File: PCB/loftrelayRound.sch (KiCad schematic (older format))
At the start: 29 parts, among them J1 PowerIn, J2 Load, J3 SenSor, J4 Program, K1 G5Q-14-EU DC5, Q1 2N7002, U1 AP1117-33, U2 PC817, U4 ESP-12E

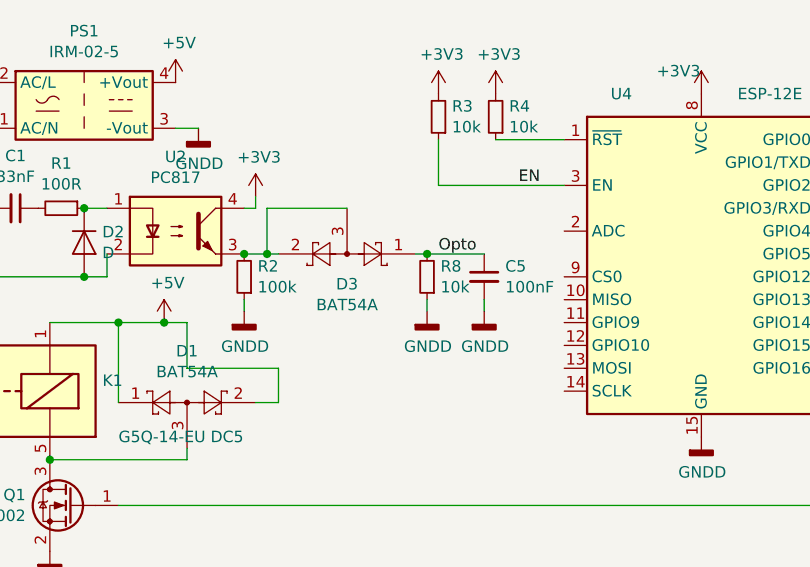
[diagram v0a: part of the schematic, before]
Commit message: Diagram rettet til
Minimeret, så overflødige komponenter er fjernet
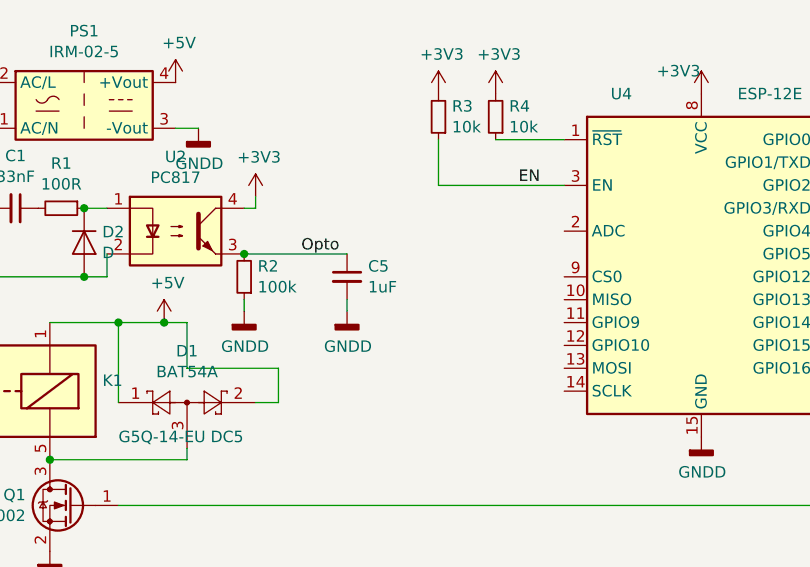
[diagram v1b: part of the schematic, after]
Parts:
- removed D3: BAT54A, Package_TO_SOT_SMD:SOT-23, symbol Diode:BAT54A
- removed R8: 10k, Resistors_SMD:R_0805_HandSoldering, symbol Device:R_Small
- C5: value 100nF -> 1uF
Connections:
- wire segments 91 -> 85
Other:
- moved on the sheet: C5
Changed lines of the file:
@@
 	1    0    0    -1
 $EndComp
-Text Label 5200 3250 0    50   ~ 0
+Text Label 4600 3250 0    50   ~ 0
 Opto
 Text Label 7000 3250 0    50   ~ 0
@@
 Wire Wire Line
 	4350 3450 4350 3500
-Wire Wire Line
-	4350 3250 4450 3250
 Connection ~ 4350 3250
-Wire Wire Line
-	5100 3250 5150 3250
-$Comp
-L Device:R_Small R8
-U 1 1 5E3364CD
-P 5150 3350
-F 0 "R8" H 5091 3304 50  0000 R CNN
-F 1 "10k" H 5091 3395 50  0000 R CNN
-F 2 "Resistors_SMD:R_0805_HandSoldering" H 5150 3350 50  0001 C CNN
-F 3 "~" H 5150 3350 50  0001 C CNN
-	1    5150 3350
-	-1   0    0    1
-$EndComp
-Connection ~ 5150 3250
-Wire Wire Line
-	5150 3250 5400 3250
 $Comp
 L Device:C_Small C5
 U 1 1 5E3365B0
-P 5400 3350
-F 0 "C5" H 5492 3396 50  0000 L CNN
-F 1 "100nF" H 5492 3305 50  0000 L CNN
-F 2 "Capacitors_SMD:C_0805_HandSoldering" H 5400 3350 50  0001 C CNN
-F 3 "~" H 5400 3350 50  0001 C CNN
-	1    5400 3350
-	1    0    0    -1
-$EndComp
-$Comp
-L power:GNDD #PWR0101
-U 1 1 5E336684
-P 5150 3500
-F 0 "#PWR0101" H 5150 3250 50  0001 C CNN
-F 1 "GNDD" H 5154 3345 50  0000 C CNN
-F 2 "" H 5150 3500 50  0001 C CNN
-F 3 "" H 5150 3500 50  0001 C CNN
-	1    5150 3500
+P 4800 3350
+F 0 "C5" H 4892 3396 50  0000 L CNN
+F 1 "1uF" H 4892 3305 50  0000 L CNN
+F 2 "Capacitors_SMD:C_0805_HandSoldering" H 4800 3350 50  0001 C CNN
+F 3 "~" H 4800 3350 50  0001 C CNN
+	1    4800 3350
 	1    0    0    -1
 $EndComp
@@
 L power:GNDD #PWR0102
 U 1 1 5E3366C3
-P 5400 3500
-F 0 "#PWR0102" H 5400 3250 50  0001 C CNN
-F 1 "GNDD" H 5404 3345 50  0000 C CNN
-F 2 "" H 5400 3500 50  0001 C CNN
-F 3 "" H 5400 3500 50  0001 C CNN
-	1    5400 3500
-	1    0    0    -1
-$EndComp
-Wire Wire Line
-	5400 3450 5400 3500
-Wire Wire Line
-	5150 3450 5150 3500
+P 4800 3500
+F 0 "#PWR0102" H 4800 3250 50  0001 C CNN
+F 1 "GNDD" H 4804 3345 50  0000 C CNN
+F 2 "" H 4800 3500 50  0001 C CNN
+F 3 "" H 4800 3500 50  0001 C CNN
+	1    4800 3500
+	1    0    0    -1
+$EndComp
+Wire Wire Line
+	4800 3450 4800 3500
 $Comp
 L power:+5V #PWR0118
@@
 	4100 4150 3500 4150
 Connection ~ 3500 4150
-$Comp
-L Diode:BAT54A D3
-U 1 1 5E35A014
-P 4800 3250
-F 0 "D3" H 4800 3382 50  0000 C CNN
-F 1 "BAT54A" H 4800 3473 50  0000 C CNN
-F 2 "Package_TO_SOT_SMD:SOT-23" H 4875 3375 50  0001 L CNN
-F 3 "http://www.diodes.com/_files/datasheets/ds11005.pdf" H 4680 3250 50  0001 C CNN
-	1    4800 3250
-	-1   0    0    1
-$EndComp
 Wire Wire Line
 	4350 3050 4400 3050
 Wire Wire Line
 	4400 3050 4400 3000
-Wire Wire Line
-	4450 3250 4450 3050
-Wire Wire Line
-	4450 3050 4800 3050
-Connection ~ 4450 3250
-Wire Wire Line
-	4450 3250 4500 3250
 Wire Wire Line
 	3800 4350 7100 4350
@@
 Wire Wire Line
 	7950 3450 8600 3450
+Wire Wire Line
+	4350 3250 4800 3250
 $EndSCHEMATC
